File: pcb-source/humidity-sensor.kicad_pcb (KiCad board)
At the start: 2 copper layers, 34.3 x 22.6 mm, 77 parts, among them J1 Conn_ARM_JTAG_SWD_10, J2 Conn_02x03_Odd_Even, Q1 Q_NMOS_GSD, Q2 Q_NMOS_GSD, U1 STM32L051C8Tx, U2 SHTC3, U3 SYN115, Y1 13.56MHz, Y2 DNU

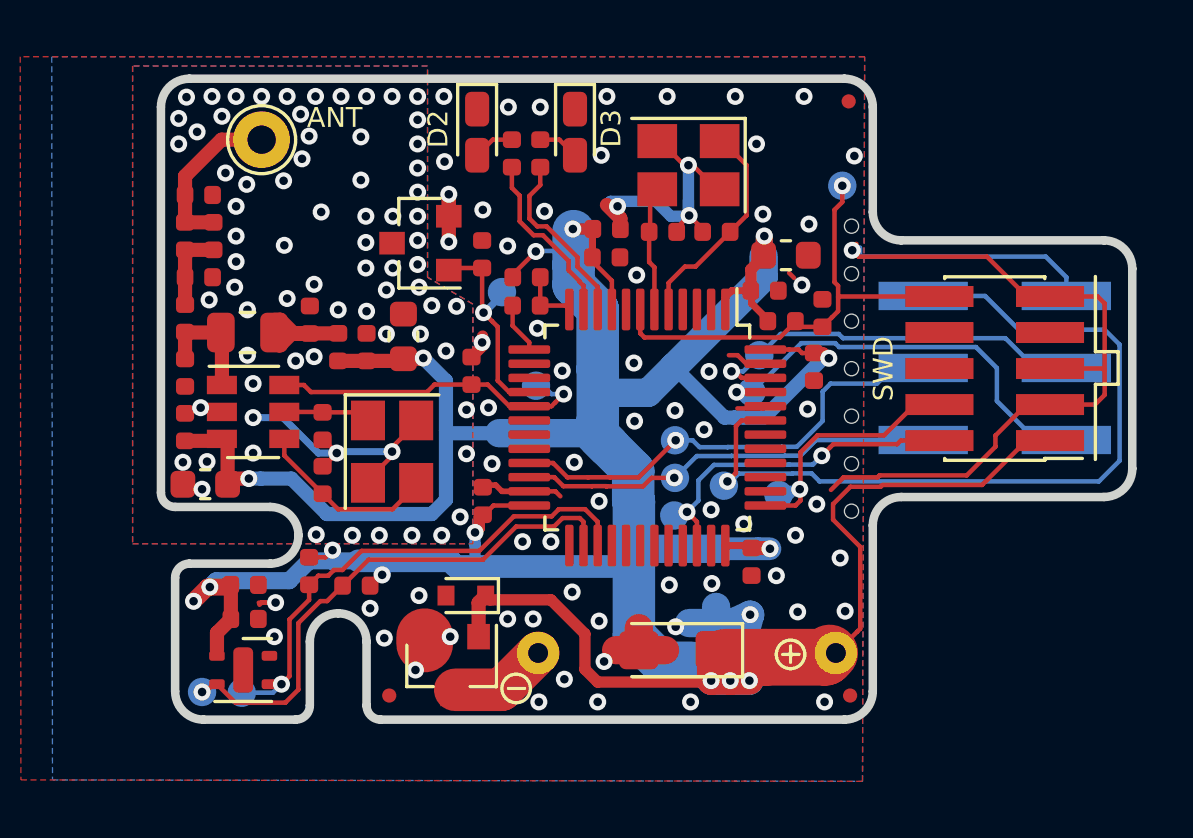
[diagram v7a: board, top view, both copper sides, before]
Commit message: Add curved RF trace, update rev template
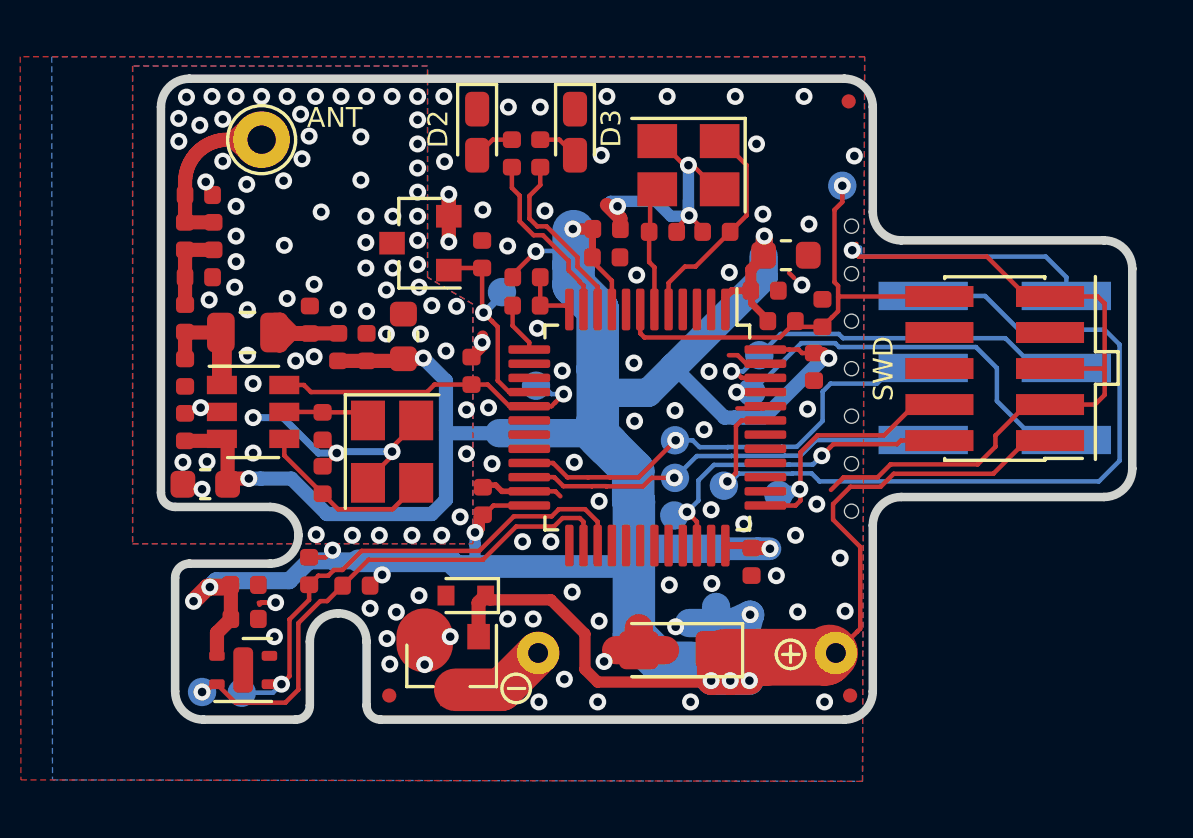
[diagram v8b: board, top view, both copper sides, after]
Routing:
- net GNDA: vias 73 -> 74
- net GND: vias 68 -> 71
